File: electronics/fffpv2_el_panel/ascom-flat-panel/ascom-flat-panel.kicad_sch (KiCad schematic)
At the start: 19 parts, among them J1 Servo, Q1 IRLZ34N, Q2 IRLZ34N, U1 XIAO-SAMD21-DIP, U2 TLC272

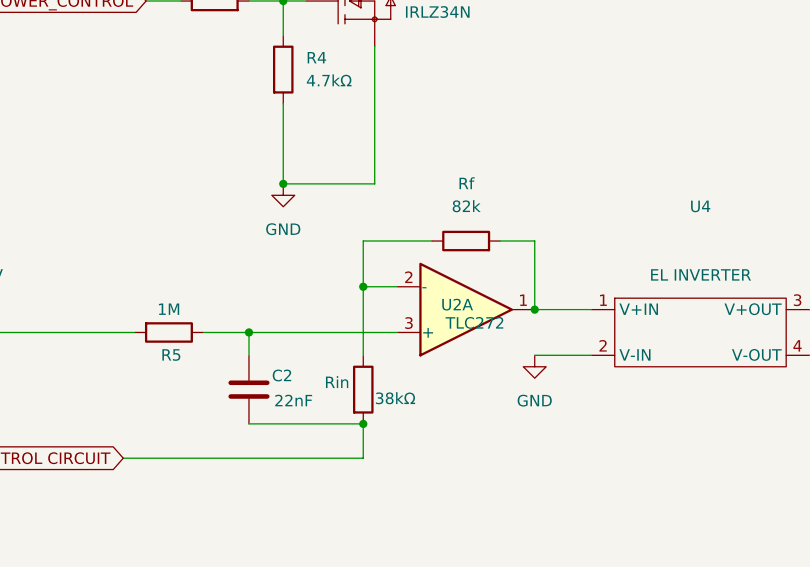
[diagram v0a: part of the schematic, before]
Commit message: [electronics] - ajout empreintes pour C2 (A CONFIRMER) et TLC272 (AOp)
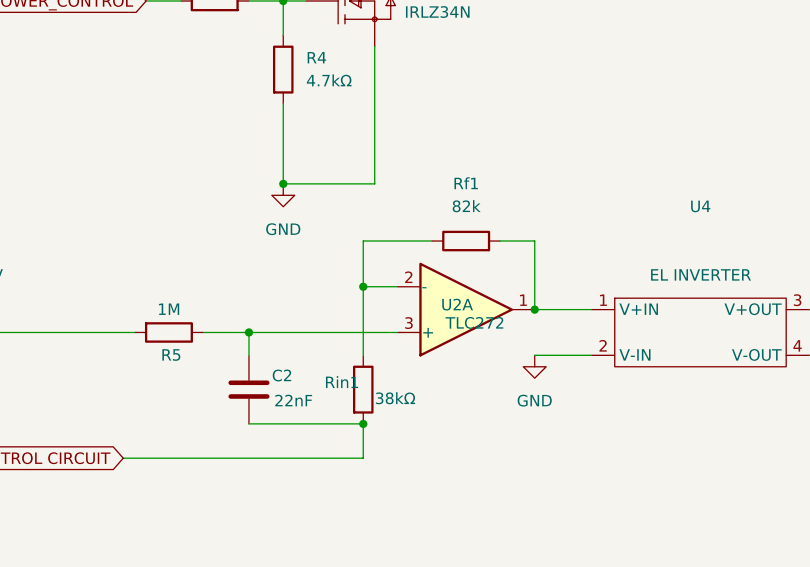
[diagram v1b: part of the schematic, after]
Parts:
- C2: footprint (none) -> Capacitor_THT:C_Disc_D3.0mm_W1.6mm_P2.50mm
- U2: footprint (none) -> Package_DIP:DIP-8_W7.62mm
- renumbered Rf to Rf1, Rin to Rin1
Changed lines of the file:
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@@
 			)
 		)
-		(property "Footprint" ""
+		(property "Footprint" "Capacitor_THT:C_Disc_D3.0mm_W1.6mm_P2.50mm"
 			(at 68.2752 149.86 0)
 			(effects
@@
 			)
 		)
-		(property "Footprint" ""
+		(property "Footprint" "Package_DIP:DIP-8_W7.62mm"
 			(at 160.02 139.7 0)
 			(effects
@@
 			)
 		)
-		(property "Footprint" ""
+		(property "Footprint" "Package_DIP:DIP-8_W7.62mm"
 			(at 91.44 137.16 0)
 			(effects
@@
 		(dnp no)
 		(fields_autoplaced yes)
-		(property "Reference" "Rf"
+		(property "Reference" "Rf1"
 			(at 91.44 123.19 90)
 			(effects
@@
 			(project "ascom-flat-panel"
 				(path "/c93103f3-9ac9-4319-baa6-df31525a6c92"
-					(reference "Rf")
+					(reference "Rf1")
 					(unit 1)
 				)
@@
 		(on_board yes)
 		(dnp no)
-		(property "Reference" "Rin"
+		(property "Reference" "Rin1"
 			(at 75.692 145.288 0)
 			(effects
@@
 			(project "ascom-flat-panel"
 				(path "/c93103f3-9ac9-4319-baa6-df31525a6c92"
-					(reference "Rin")
-					(unit 1)
-				)
+					(reference "Rin1")
+					(unit 1)
+				)

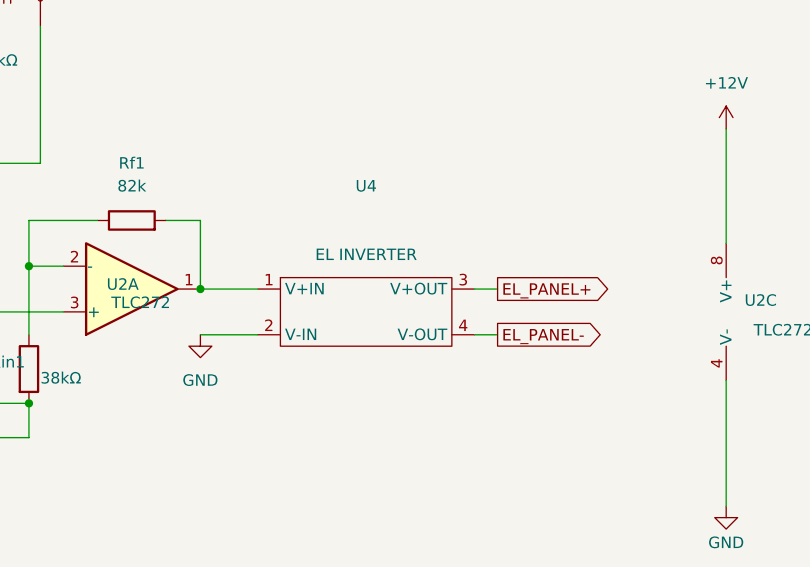
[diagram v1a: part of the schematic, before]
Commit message: [electronics] - supression de l'inverter du schema, car pas connecté par pistes sur pcb [TO DO : prevoir connecteur ou pads pour souder cables)
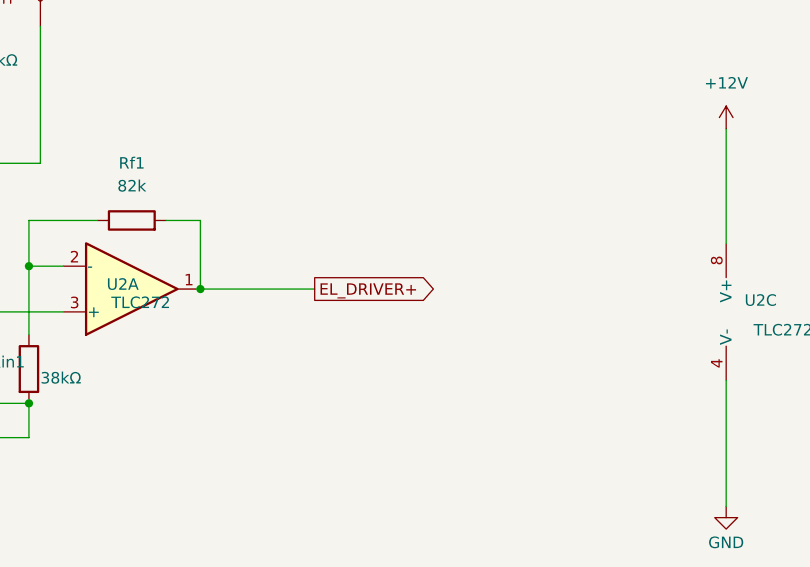
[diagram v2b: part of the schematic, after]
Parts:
- removed U4: ~, CustomFootprints:DFR052 DC regulator, symbol CustomSymbols:EL_INVERTER
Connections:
- net EL_DRIVER+: now reaches Rf1.2, U2.1
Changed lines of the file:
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@@
+	)
+	(junction
+		(at 232.41 91.44)
+		(diameter 0)
+		(color 0 0 0 0)
+	)
+	(junction
+		(at 80.01 149.86)
+		(diameter 0)
+		(color 0 0 0 0)
 	)
 	(junction
@@
 		(color 0 0 0 0)
 	)
-	(junction
-		(at 232.41 91.44)
-		(diameter 0)
-		(color 0 0 0 0)
-	)
-	(junction
-		(at 80.01 149.86)
-		(diameter 0)
-		(color 0 0 0 0)
-	)
 	(wire
 		(pts
@@
 	(wire
 		(pts
-			(xy 99.06 142.24) (xy 105.41 142.24)
-		)
-		(stroke
-			(width 0)
-			(type default)
-		)
-	)
-	(wire
-		(pts
-			(xy 129.54 137.16) (xy 132.08 137.16)
-		)
-		(stroke
-			(width 0)
-			(type default)
-		)
-	)
-	(wire
-		(pts
 			(xy 157.48 119.38) (xy 157.48 132.08)
 		)
@@
 	(wire
 		(pts
-			(xy 129.54 142.24) (xy 132.08 142.24)
-		)
-		(stroke
-			(width 0)
-			(type default)
-		)
-	)
-	(wire
-		(pts
 			(xy 105.41 63.5) (xy 115.57 63.5)
 		)
@@
 	(wire
 		(pts
+			(xy 99.06 137.16) (xy 111.76 137.16)
+		)
+		(stroke
+			(width 0)
+			(type default)
+		)
+	)
+	(wire
+		(pts
 			(xy 54.61 59.69) (xy 63.5 59.69)
-		)
-		(stroke
-			(width 0)
-			(type default)
-		)
-	)
-	(wire
-		(pts
-			(xy 99.06 137.16) (xy 105.41 137.16)
 		)
 		(stroke
@@
 		)
 	)
-	(global_label "EL_PANEL+"
+	(global_label "EL_DRIVER+"
 		(shape output)
-		(at 132.08 137.16 0)
+		(at 111.76 137.16 0)
 		(fields_autoplaced yes)
 		(effects
@@
 		)
 		(property "Intersheetrefs" "${INTERSHEET_REFS}"
-			(at 145.6485 137.16 0)
+			(at 126.1147 137.16 0)
 			(effects
 				(font
@@
 		)
 	)
-	(global_label "EL_PANEL-"
-		(shape output)
-		(at 132.08 142.24 0)
+	(global_label "SERVO GND"
+		(shape input)
+		(at 197.866 61.214 0)
 		(fields_autoplaced yes)
 		(effects
@@
 		)
 		(property "Intersheetrefs" "${INTERSHEET_REFS}"
-			(at 145.6485 142.24 0)
+			(at 211.7369 61.214 0)
 			(effects
 				(font
@@
 	(global_label "SERVO GND"
 		(shape input)
-		(at 197.866 61.214 0)
+		(at 247.142 66.294 0)
 		(fields_autoplaced yes)
 		(effects
@@
 		)
 		(property "Intersheetrefs" "${INTERSHEET_REFS}"
-			(at 211.7369 61.214 0)
+			(at 261.0129 66.294 0)
 			(effects
 				(font
@@
 		)
 	)
-	(global_label "SERVO GND"
-		(shape input)
-		(at 247.142 66.294 0)
-		(fields_autoplaced yes)
-		(effects
-			(font
-				(size 1.27 1.27)
-			)
-			(justify left)
-		)
-		(property "Intersheetrefs" "${INTERSHEET_REFS}"
-			(at 261.0129 66.294 0)
-			(effects
-				(font
-					(size 1.27 1.27)
-				)
-				(justify left)
-				(hide yes)
-			)
-		)
-	)
 	(global_label "LED_STRIP_POWER_CONTROL"
 		(shape input)
@@
 				(justify right)
 				(hide yes)
-			)
-		)
-	)
-	(symbol
-		(lib_id "CustomSymbols:EL_INVERTER")
-		(at 118.11 139.7 0)
-		(unit 1)
-		(exclude_from_sim no)
-		(in_bom yes)
-		(on_board yes)
-		(dnp no)
-		(fields_autoplaced yes)
-		(property "Reference" "U4"
-			(at 117.475 125.73 0)
-			(effects
-				(font
-					(size 1.27 1.27)
-				)
-			)
-		)
-		(property "Value" "~"
-			(at 117.475 128.27 0)
-			(effects
-				(font
-					(size 1.27 1.27)
-				)
-			)
-		)
-		(property "Footprint" "CustomFootprints:DFR052 DC regulator"
-			(at 118.11 139.7 0)
-			(effects
-				(font
-					(size 1.27 1.27)
-				)
-				(hide yes)
-			)
-		)
-		(property "Datasheet" "https://www.dfrobot.com/product-2584.html"
-			(at 117.475 130.81 0)
-			(effects
-				(font
-					(size 1.27 1.27)
-				)
-				(hide yes)
-			)
-		)
-		(property "Description" "EL INVERTER"
-			(at 117.475 133.35 0)
-			(effects
-				(font
-					(size 1.27 1.27)
-				)
-			)
-		)
-		(pin "4"
-		)
-		(pin "1"
-		)
-		(pin "2"
-		)
-		(pin "3"
-		)
-		(instances
-			(project ""
-				(path "/c93103f3-9ac9-4319-baa6-df31525a6c92"
-					(reference "U4")
-					(unit 1)
-				)
 			)
 		)
@@
 					(unit 1)
 				)
-			)
-		)
-	)
-	(symbol
-		(lib_name "GND_4")
-		(lib_id "power:GND")
-		(at 99.06 142.24 0)
-		(unit 1)
-		(exclude_from_sim no)
-		(in_bom yes)
-		(on_board yes)
-		(dnp no)
-		(fields_autoplaced yes)
-		(property "Reference" "#PWR019"
-			(at 99.06 148.59 0)
-			(effects
-				(font
-					(size 1.27 1.27)
-				)
-				(hide yes)
-			)
-		)
-		(property "Value" "GND"
-			(at 99.06 147.32 0)
-			(effects
-				(font
-					(size 1.27 1.27)
-				)
-			)
-		)
-		(property "Footprint" ""
-			(at 99.06 142.24 0)
-			(effects
-				(font
-					(size 1.27 1.27)
-				)
-				(hide yes)
-			)
-		)
-		(property "Datasheet" ""
-			(at 99.06 142.24 0)
-			(effects
-				(font
-					(size 1.27 1.27)
-				)
-				(hide yes)
-			)
-		)
-		(property "Description" "Power symbol creates a global label with name \"GND\" , ground"
-			(at 99.06 142.24 0)
-			(effects
-				(font
-					(size 1.27 1.27)
-				)
-				(hide yes)
-			)
-		)
-		(pin "1"
-		)
-		(instances
-			(project ""
-				(path "/c93103f3-9ac9-4319-baa6-df31525a6c92"
-					(reference "#PWR019")
-					(unit 1)
-				)

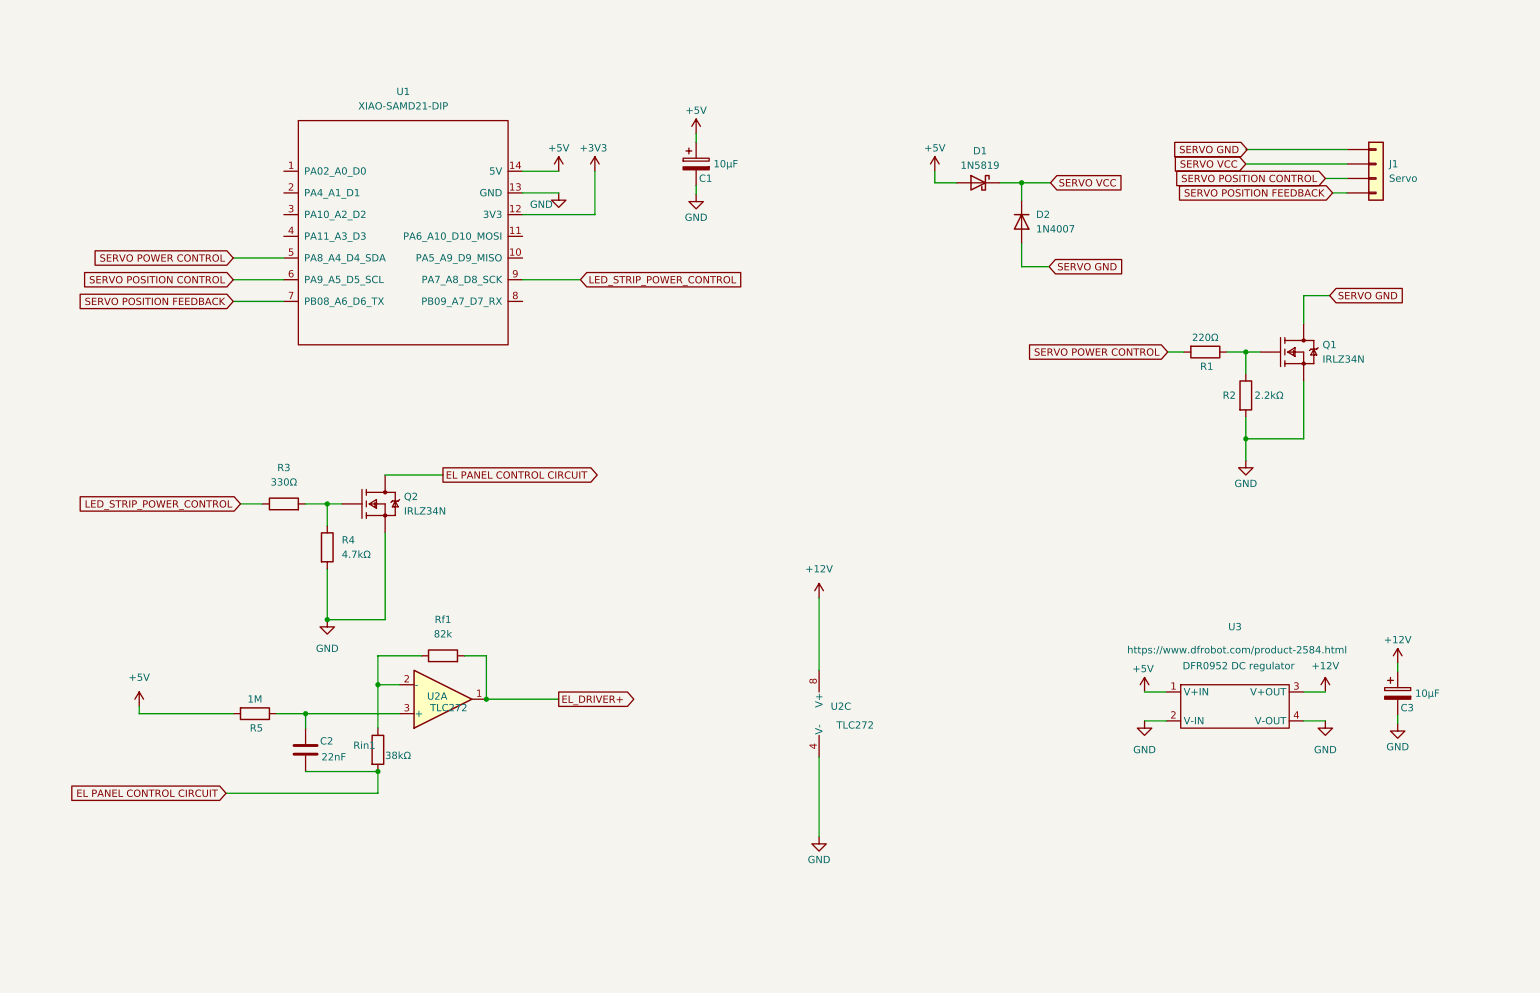
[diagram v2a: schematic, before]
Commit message: Added connector to EL Driver
- No footprint associated
- Just schematics
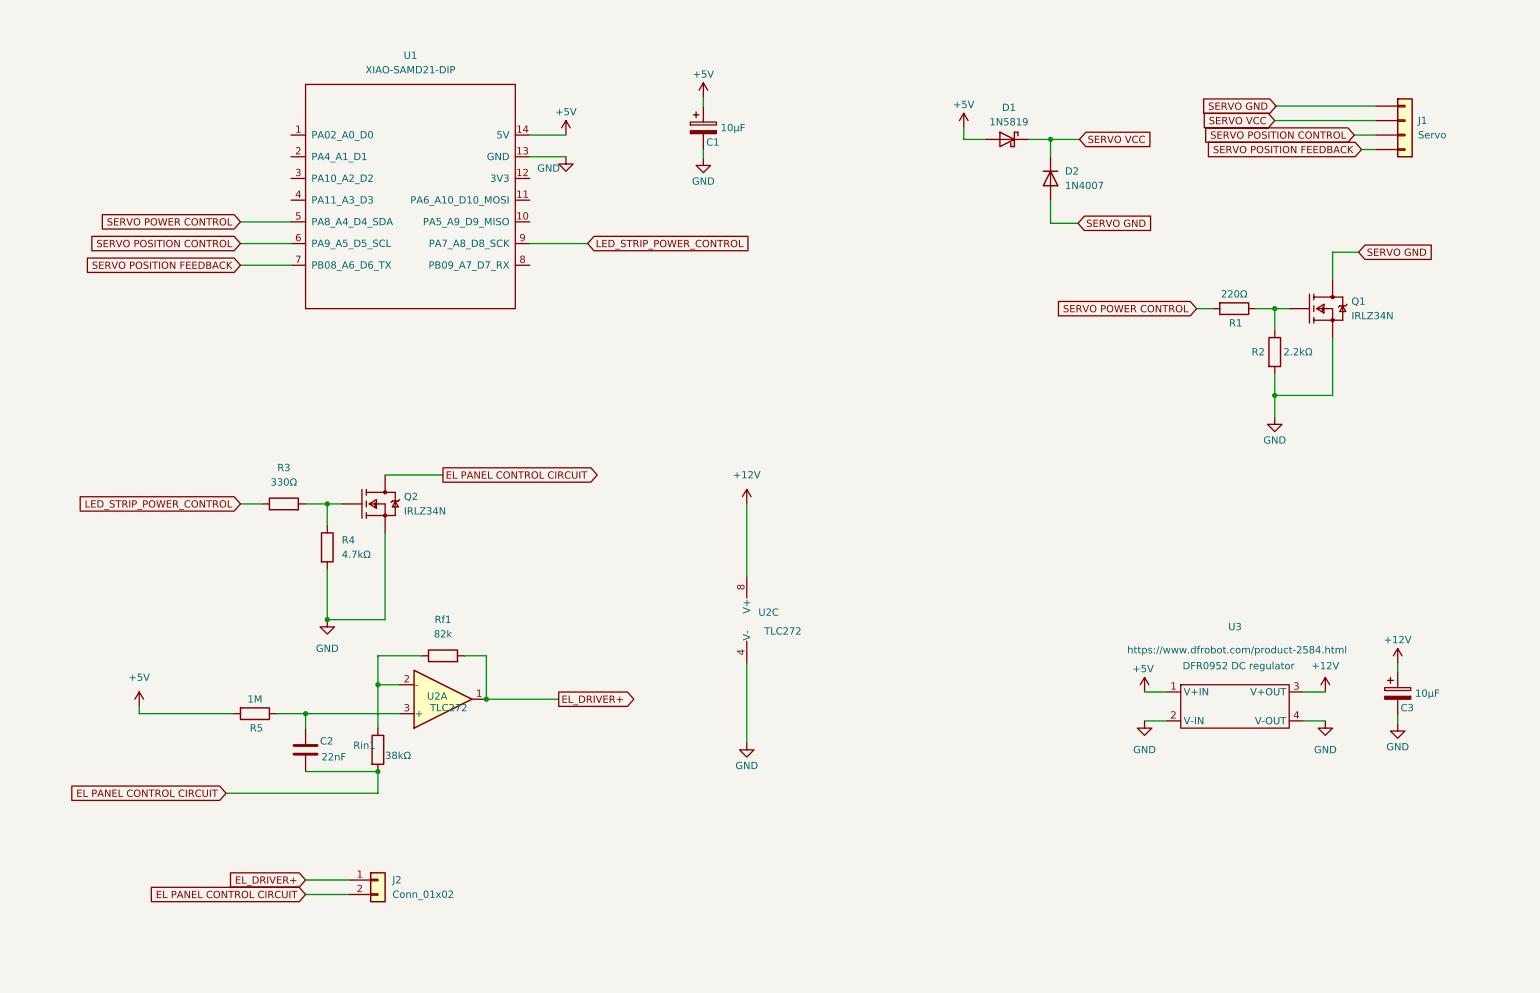
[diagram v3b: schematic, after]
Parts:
- added J2: Conn_01x02, symbol Connector_Generic:Conn_01x02
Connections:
- net EL PANEL CONTROL CIRCUIT: now also J2.2 (Pin_2)
- net EL_DRIVER+: now also J2.1 (Pin_1)
- net +3V3: no longer names the net of U1.12 (3V3)
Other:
- moved on the sheet: C1, D1, D2, J1, Q1, R1, R2, U1, U2C

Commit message: ajout d'une empreinte pour le connecteur JST en direction de l'inverter. Je laisse le pro du routage câbler ça j'ai peur de tout péter :D
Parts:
- J2: footprint (none) -> Connector_JST:JST_XH_B2B-XH-A_1x02_P2.50mm_Vertical
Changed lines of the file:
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@@
 			)
 		)
-		(property "Footprint" ""
+		(property "Footprint" "Connector_JST:JST_XH_B2B-XH-A_1x02_P2.50mm_Vertical"
 			(at 80.01 168.91 0)
 			(effects

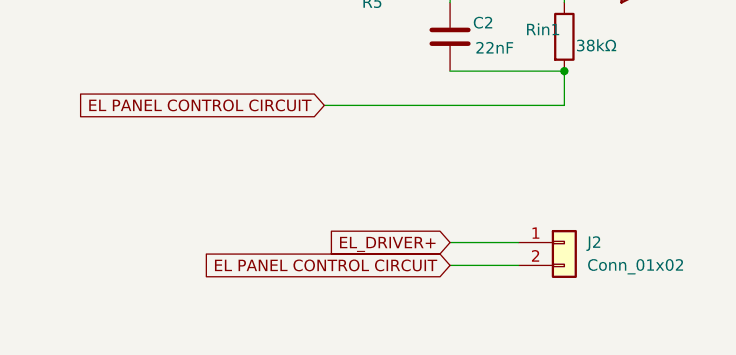
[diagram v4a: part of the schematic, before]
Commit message: EL driver '-' pin should be grounded
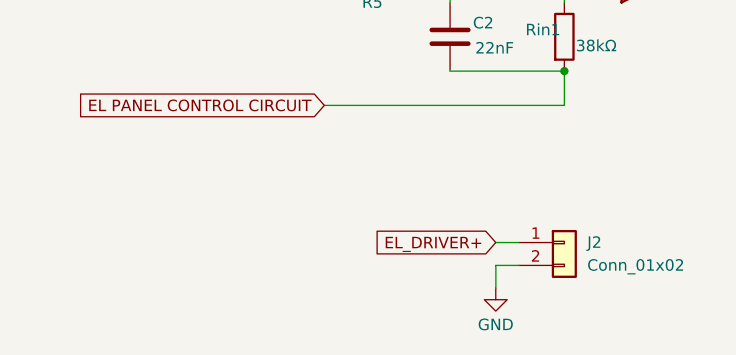
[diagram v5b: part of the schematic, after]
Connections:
- net EL PANEL CONTROL CIRCUIT: no longer J2.2 (Pin_2)
- net GND: now also J2.2 (Pin_2)
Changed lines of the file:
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@@
 	(wire
 		(pts
-			(xy 67.31 171.45) (xy 74.93 171.45)
+			(xy 237.49 35.56) (xy 255.27 35.56)
 		)
 		(stroke
@@
 	(wire
 		(pts
-			(xy 237.49 35.56) (xy 255.27 35.56)
+			(xy 55.88 60.96) (xy 64.77 60.96)
 		)
 		(stroke
@@
 	(wire
 		(pts
-			(xy 55.88 60.96) (xy 64.77 60.96)
+			(xy 81.28 107.95) (xy 81.28 123.19)
 		)
 		(stroke
@@
 	(wire
 		(pts
-			(xy 81.28 107.95) (xy 81.28 123.19)
+			(xy 106.68 41.91) (xy 113.03 41.91)
 		)
 		(stroke
@@
 	(wire
 		(pts
-			(xy 106.68 41.91) (xy 113.03 41.91)
+			(xy 72.39 173.99) (xy 72.39 171.45)
+		)
+		(stroke
+			(width 0)
+			(type default)
+		)
+	)
+	(wire
+		(pts
+			(xy 72.39 171.45) (xy 74.93 171.45)
 		)
 		(stroke
@@
 	(wire
 		(pts
-			(xy 67.31 168.91) (xy 74.93 168.91)
+			(xy 72.39 168.91) (xy 74.93 168.91)
 		)
 		(stroke
@@
 		)
 	)
-	(global_label "EL PANEL CONTROL CIRCUIT"
-		(shape input)
-		(at 67.31 171.45 180)
-		(fields_autoplaced yes)
-		(effects
-			(font
-				(size 1.27 1.27)
-			)
-			(justify right)
-		)
-		(property "Intersheetrefs" "${INTERSHEET_REFS}"
-			(at 37.5338 171.45 0)
-			(effects
-				(font
-					(size 1.27 1.27)
-				)
-				(justify right)
-				(hide yes)
-			)
-		)
-	)
 	(global_label "SERVO GND"
 		(shape input)
@@
 	(global_label "EL_DRIVER+"
 		(shape input)
-		(at 67.31 168.91 180)
+		(at 72.39 168.91 180)
 		(fields_autoplaced yes)
 		(effects
@@
 		)
 		(property "Intersheetrefs" "${INTERSHEET_REFS}"
-			(at 52.9553 168.91 0)
+			(at 58.0353 168.91 0)
 			(effects
 				(font
@@
 					(unit 1)
 				)
+			)
+		)
+	)
+	(symbol
+		(lib_id "power:GND")
+		(at 72.39 173.99 0)
+		(unit 1)
+		(exclude_from_sim no)
+		(in_bom yes)
+		(on_board yes)
+		(dnp no)
+		(property "Reference" "#PWR06"
+			(at 72.39 180.34 0)
+			(effects
+				(font
+					(size 1.27 1.27)
+				)
+				(hide yes)
+			)
+		)
+		(property "Value" "GND"
+			(at 72.39 178.054 0)
+			(effects
+				(font
+					(size 1.27 1.27)
+				)
+			)
+		)
+		(property "Footprint" ""
+			(at 72.39 173.99 0)
+			(effects
+				(font
+					(size 1.27 1.27)
+				)
+				(hide yes)
+			)
+		)
+		(property "Datasheet" ""
+			(at 72.39 173.99 0)
+			(effects
+				(font
+					(size 1.27 1.27)
+				)
+				(hide yes)
+			)
+		)
+		(property "Description" ""
+			(at 72.39 173.99 0)
+			(effects
+				(font
+					(size 1.27 1.27)
+				)
+			)
+		)
+		(pin "1"
+		)
+		(instances
+			(project "ascom-flat-panel"
+				(path "/c93103f3-9ac9-4319-baa6-df31525a6c92"
+					(reference "#PWR06")
+					(unit 1)
+				)
